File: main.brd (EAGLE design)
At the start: 400 x 300 mm, 474 parts, among them J100 DCJ0202, Q200 NMOS, Q201 PMOS, Q300 PMOS, Q400 PMOS, U100 NE555N, U1000 74LS173N, U1001 74LS173N, U1002 74LS245N, U1003 74LS173N, U1004 74LS173N, U1005 74LS245N, U101 NE555N, U102 NE555N, U103 74LS04N, U104 74LS08N, U105 74LS32N, U1100 74LS173N, U1101 74LS173N, U1102 74LS161N, U1106 74HCT154DW, U1107 74HCT154DW, U1108 74LS04N, U1109 74LS04N, U200 HM62256, U201 74LS173N, U202 74LS173N, U203 74LS173N, U204 74LS173N, U205 74LS157N, U206 74LS157N, U207 74LS157N, U208 74LS157N, U209 74HCT595D, U210 74HCT595D, U211 74HCT595D, U212 74LS245N, U213 74LS245N, U214 74LS00N, U215 74LS173N, U216 74LS173N, U217 74LS173N, U218 74LS173N, U219 74LS245N, U220 74LS245N, U300 74LS299N, U301 74LS245N, U302 74LS08N, U303 74LS00N, U304 74LS245N, U400 74LS00N, U401 74LS245N, U500 74LS161N, U501 74LS161N, U502 74LS161N, U503 74LS161N, U504 74LS245N, U505 74LS245N, U600 74LS173N, U601 74LS173N, U602 74LS173N, U603 74LS173N, U604 74LS245N, U700 74LS283N, U701 74LS283N, U702 74LS245N, U703 74LS86N, U704 74LS86N, U705 74LS85N, U706 74LS85N, U707 74LS173N, U708 74LS125N, U800 74LS04N, U801 74LS04N, U802 74LS08N, U803 74LS08N, U804 74LS32N, U805 74LS32N, U806 74LS86N, U807 74LS86N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

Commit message: Moved ResNet to included library.
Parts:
- RN1000, RN1001, RN1100, RN1101, RN1102, RN1103, RN1104, RN1105, RN1106, RN1107, RN200, RN201, RN202, RN203, RN204, RN205, RN206, RN207, RN300, RN301, RN302, RN400, RN500, RN501, RN600, RN601, RN700, RN800, RN900: device SamacSys_Parts:CAY16102J8LF -> 8BitCpuParts:CAY16102J8LF

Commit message: Some work on OUT module.
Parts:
- moved C907 80.8 mm to (148.6, 92.7), flipped to the bottom, turned to 180 degrees
- moved C908 79.4 mm to (143.5, 89.9), flipped to the bottom, turned to 90 degrees
- moved R904 66.5 mm to (165.6, 94.7), flipped to the bottom, turned to 180 degrees
- moved R903 58.9 mm to (161.3, 94.7), flipped to the bottom, turned to 180 degrees
- moved C900 54.6 mm to (151.5, 92.1), flipped to the bottom, turned to 90 degrees
- moved R902 51.4 mm to (157.0, 94.7), flipped to the bottom, turned to 180 degrees
- moved R901 38.6 mm to (146.6, 89.2), flipped to the bottom
- moved R900 38.0 mm to (150.6, 89.2), flipped to the bottom
- moved LED900 8.89 mm to (156.7, 92.7)
- moved LED902 8.89 mm to (165.4, 92.7)
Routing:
- net GND: track 2024.9 -> 2152.9 mm
- net OUT_SEG_A: track 0.00 -> 77.0 mm, vias 0 -> 3
- net OUT_SEG_B: track 0.00 -> 73.9 mm, vias 0 -> 3
- net VCC: track 1562.9 -> 1636.7 mm
- net OUT_MODE_1: track 0.00 -> 70.0 mm, vias 0 -> 1
- net OUT_MODE_0: track 0.00 -> 68.8 mm, vias 0 -> 1
- net OUT_SEG_F: track 0.00 -> 65.8 mm, vias 0 -> 3
- net OUT_MUX_0: track 0.00 -> 63.6 mm
- net OUT_SEG_G: track 0.00 -> 62.7 mm
- net OUT_MUX_1: track 0.00 -> 62.1 mm, vias 0 -> 1
- net OUT_MODE_2: track 0.00 -> 60.8 mm
- net OUT_CAT_0: track 0.00 -> 55.9 mm, vias 0 -> 1
- net OUT_SEG_C: track 0.00 -> 55.6 mm, vias 0 -> 3
- net OUT_SEG_DP: track 0.00 -> 52.8 mm, vias 0 -> 3
- net OUT_SEG_D: track 0.00 -> 49.9 mm, vias 0 -> 3
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
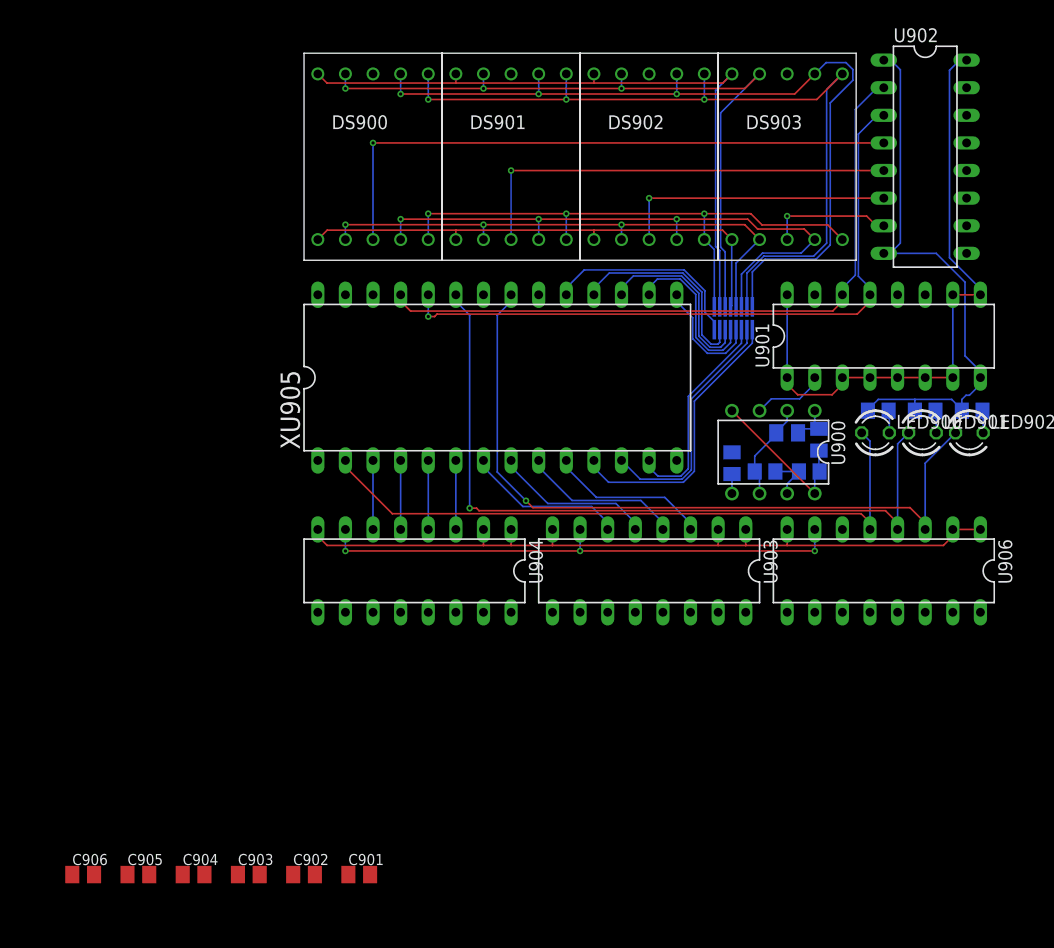
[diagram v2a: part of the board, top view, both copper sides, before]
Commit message: Finished OUT module.
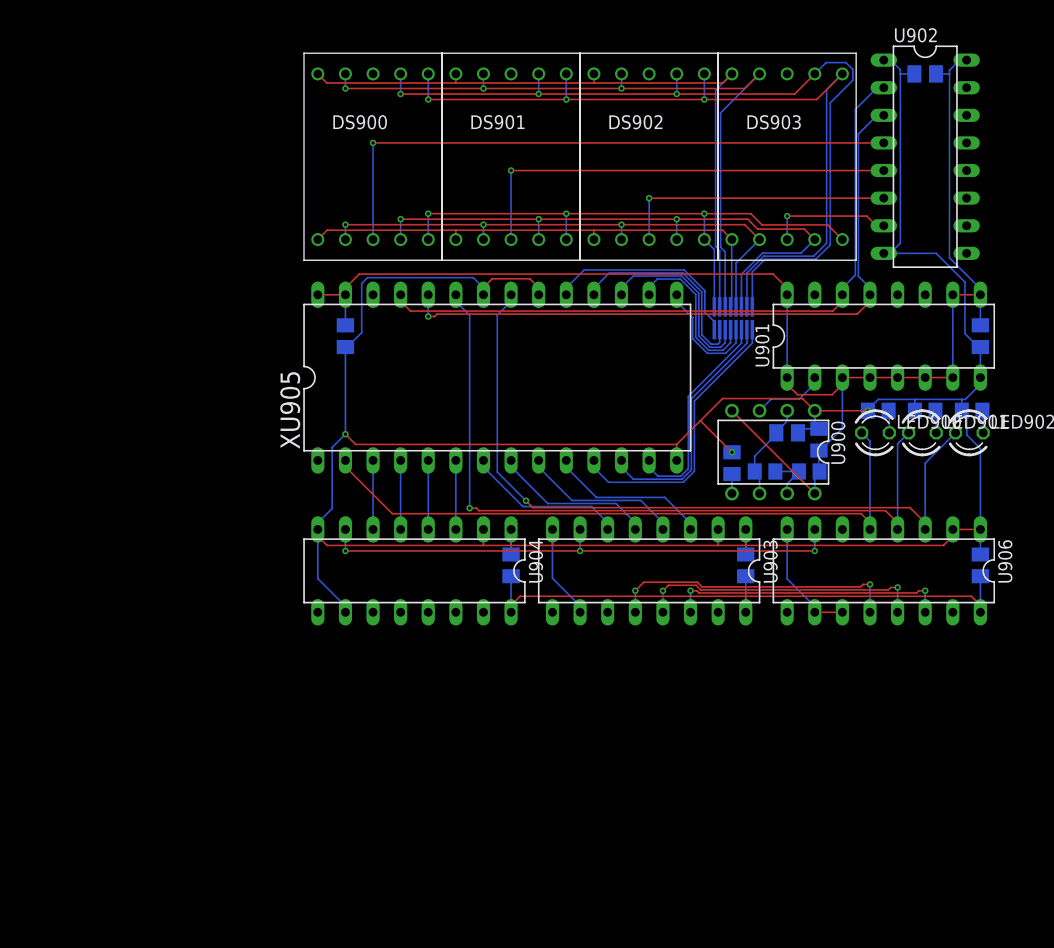
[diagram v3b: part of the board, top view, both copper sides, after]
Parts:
- moved C902 93.2 mm to (161.3, 125.7), flipped to the bottom
- moved C906 87.3 mm to (166.4, 80.5), flipped to the bottom, turned to 90 degrees
- moved C901 75.6 mm to (166.4, 101.6), flipped to the bottom, turned to 270 degrees
- moved C903 53.8 mm to (144.8, 80.5), flipped to the bottom, turned to 90 degrees
- moved C905 53.1 mm to (108.0, 101.6), flipped to the bottom, turned to 270 degrees
- moved C904 40.8 mm to (123.2, 80.5), flipped to the bottom, turned to 90 degrees
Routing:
- net GND: track 2152.9 -> 2301.0 mm, vias 26 -> 29
- net VCC: track 1636.7 -> 1753.3 mm
- net MAINBUS_2: track 430.5 -> 457.2 mm, vias 4 -> 6
- net MAINBUS_1: track 441.3 -> 467.6 mm, vias 4 -> 6
- net MAINBUS_0: track 450.5 -> 476.3 mm, vias 2 -> 4

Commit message: CMP Beginnings
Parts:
- moved C706 34.3 mm to (270.5, 243.8), flipped to the bottom, turned to 270 degrees
- moved C708 31.8 mm to (262.9, 242.6), flipped to the bottom
- moved C707 17.1 mm to (288.3, 256.5), flipped to the bottom, turned to 90 degrees
- flipped C705 to the bottom, turned to 270 degrees
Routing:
- net GND: track 2301.0 -> 2388.9 mm, vias 29 -> 30
- net GT: track 0.00 -> 51.1 mm
- net EQ: track 0.00 -> 51.0 mm
- net CA: track 0.00 -> 49.0 mm
- net LT: track 0.00 -> 39.1 mm
- net CMP_<_CARRY: track 0.00 -> 36.8 mm
- net CMP_=_CARRY: track 0.00 -> 31.4 mm
- net CMP_>_CARRY: track 0.00 -> 26.1 mm
- net CMP_<: track 0.00 -> 13.8 mm
- net CMP_>: track 0.00 -> 13.8 mm
- net CMP_=: track 0.00 -> 13.8 mm
- net VCC: track 1753.3 -> 1766.6 mm
- net LED711_GND: track 0.00 -> 2.86 mm
- net LED710_GND: track 0.00 -> 2.86 mm
- net LED709_GND: track 0.00 -> 2.86 mm
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
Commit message: Arranged modules, some bus connections.
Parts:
- moved C901 143.5 mm to (199.4, 241.3)
- moved C905 143.5 mm to (141.0, 241.3)
- moved C908 143.5 mm to (176.5, 229.6)
- moved R900 143.5 mm to (183.6, 228.9)
- moved R901 143.5 mm to (179.6, 228.9)
- moved U901 143.5 mm to (190.5, 241.3)
- moved C900 143.5 mm to (184.5, 231.8)
- moved C902 143.5 mm to (194.3, 265.4)
- moved C903 143.5 mm to (177.8, 220.2)
- moved C904 143.5 mm to (156.2, 220.2)
- moved C906 143.5 mm to (199.4, 220.2)
- moved C907 143.5 mm to (181.6, 232.4)
- moved DS900 143.5 mm to (143.5, 257.8)
- moved DS901 143.5 mm to (156.2, 257.8)
- moved DS902 143.5 mm to (168.9, 257.8)
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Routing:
- net REG_A_1: track 100.2 -> 261.8 mm, vias 1 -> 4
- net REG_A_0: track 97.6 -> 257.8 mm, vias 0 -> 1
- net REG_A_2: track 113.6 -> 259.2 mm, vias 2 -> 3
- net REG_A_4: track 85.8 -> 227.1 mm, vias 1 -> 2
- net REG_A_3: track 120.1 -> 253.4 mm, vias 1 -> 2
- net REG_A_5: track 88.5 -> 219.2 mm, vias 1 -> 2
- net REG_B_0: track 53.0 -> 183.1 mm, vias 2 -> 3
- net MAINBUS_0: track 476.3 -> 601.3 mm
- net REG_B_1: track 43.7 -> 166.9 mm, vias 0 -> 5
- net MAINBUS_7: track 345.9 -> 469.0 mm, vias 5 -> 6
- net MAINBUS_4: track 388.0 -> 509.0 mm
- net MAINBUS_6: track 371.6 -> 492.3 mm
- net MAINBUS_5: track 382.5 -> 501.7 mm
- net REG_A_6: track 101.0 -> 218.7 mm, vias 2 -> 4
- net REG_B_4: track 51.0 -> 154.7 mm, vias 2 -> 5
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
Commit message: Most inter-module connections done, added RESET.
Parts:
- moved U303 485.3 mm to (126.4, 230.3)
- moved S300 475.2 mm to (124.1, 219.8)
- moved R300 474.3 mm to (118.7, 230.3), flipped to the bottom, turned to 90 degrees
- moved C303 463.2 mm to (134.0, 230.3), flipped to the bottom, turned to 270 degrees
- moved RN302 56.9 mm to (247.7, 656.6)
- moved R400 12.5 mm to (100.8, 195.3), flipped to the bottom, turned to 180 degrees
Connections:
- new net !CLK: U1102.2
- net CLK: no longer U1102.2
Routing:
- net CLK: track 534.1 -> 657.9 mm, vias 16 -> 19
- net MAINBUS_0: track 601.3 -> 721.4 mm
- net VCC: track 1818.3 -> 1921.4 mm, vias 32 -> 34
- net MAINBUS_2: track 553.7 -> 648.3 mm
- net MAINBUS_1: track 563.9 -> 658.5 mm
- net MAINBUS_3: track 515.8 -> 607.3 mm
- net MAINBUS_5: track 501.7 -> 580.9 mm
- net MAINBUS_6: track 492.3 -> 570.2 mm
- net MAINBUS_4: track 509.0 -> 586.7 mm
- net MAINBUS_7: track 469.0 -> 546.3 mm
- net GND: track 2413.7 -> 2488.3 mm, vias 32 -> 34
- net ALU_CARRY_OVER: track 0.00 -> 70.9 mm, vias 0 -> 2
- net RST: track 141.9 -> 205.3 mm, vias 2 -> 3
- net RMSB_INT: track 23.6 -> 85.3 mm, vias 0 -> 2
- net !CMP_EQ_OUT: track 0.00 -> 56.6 mm
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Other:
- board text added: "RESET"
